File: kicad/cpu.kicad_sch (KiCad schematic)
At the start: 26 parts, among them U1 8288, U2 74LS245, U21 74LS92, U22 74LS245, U23 8087, U24 8088, U28 8237, U29 8255A, U43 74LS74, U45 74LS04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

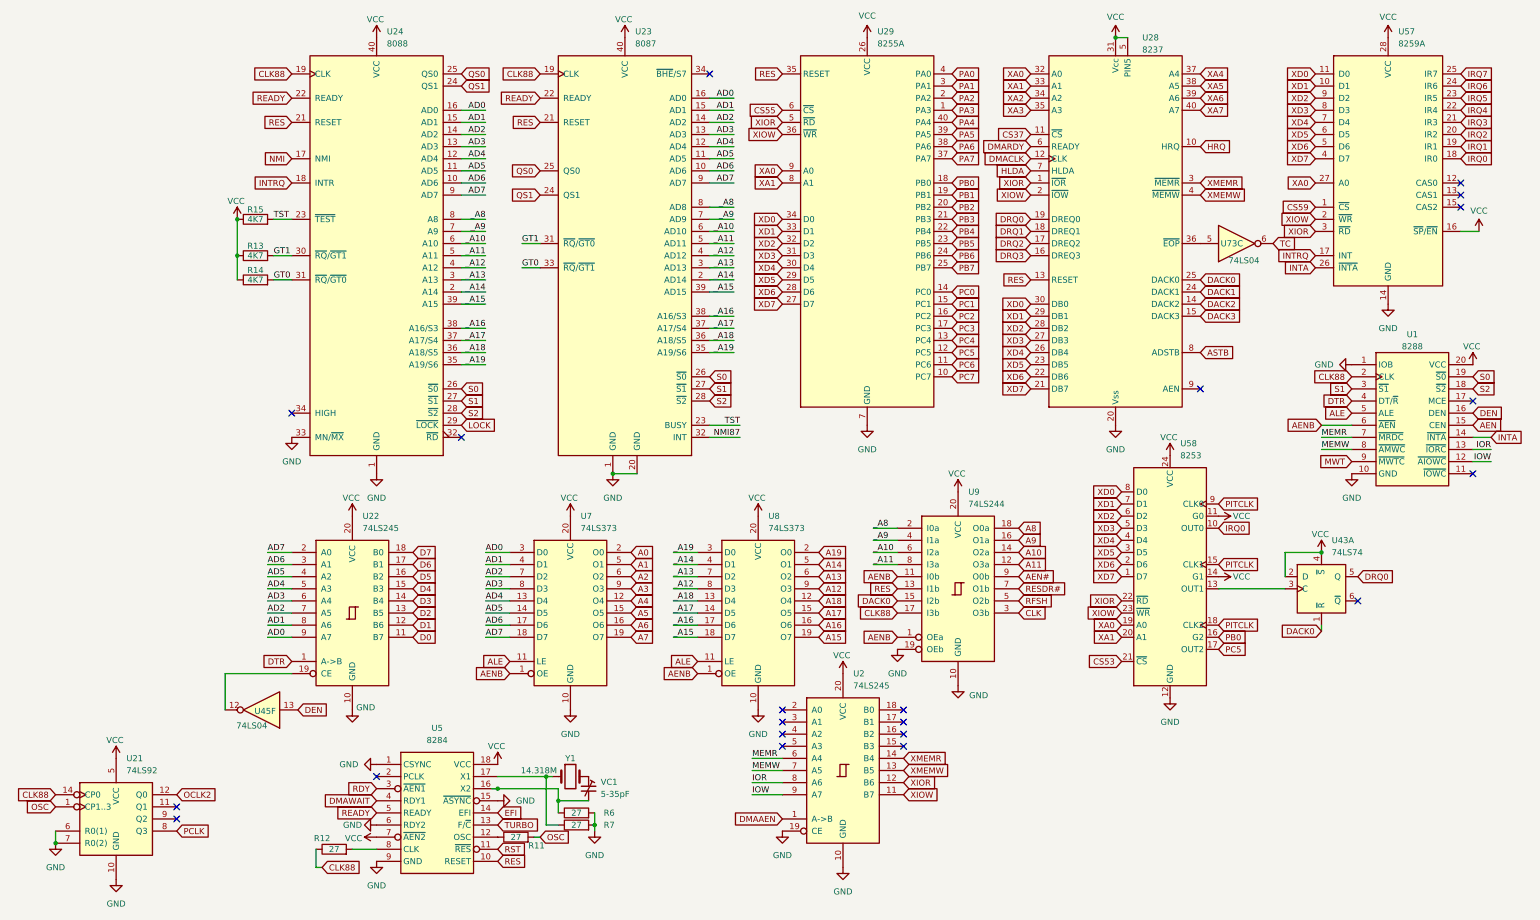
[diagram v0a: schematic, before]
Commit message: finalized schematic
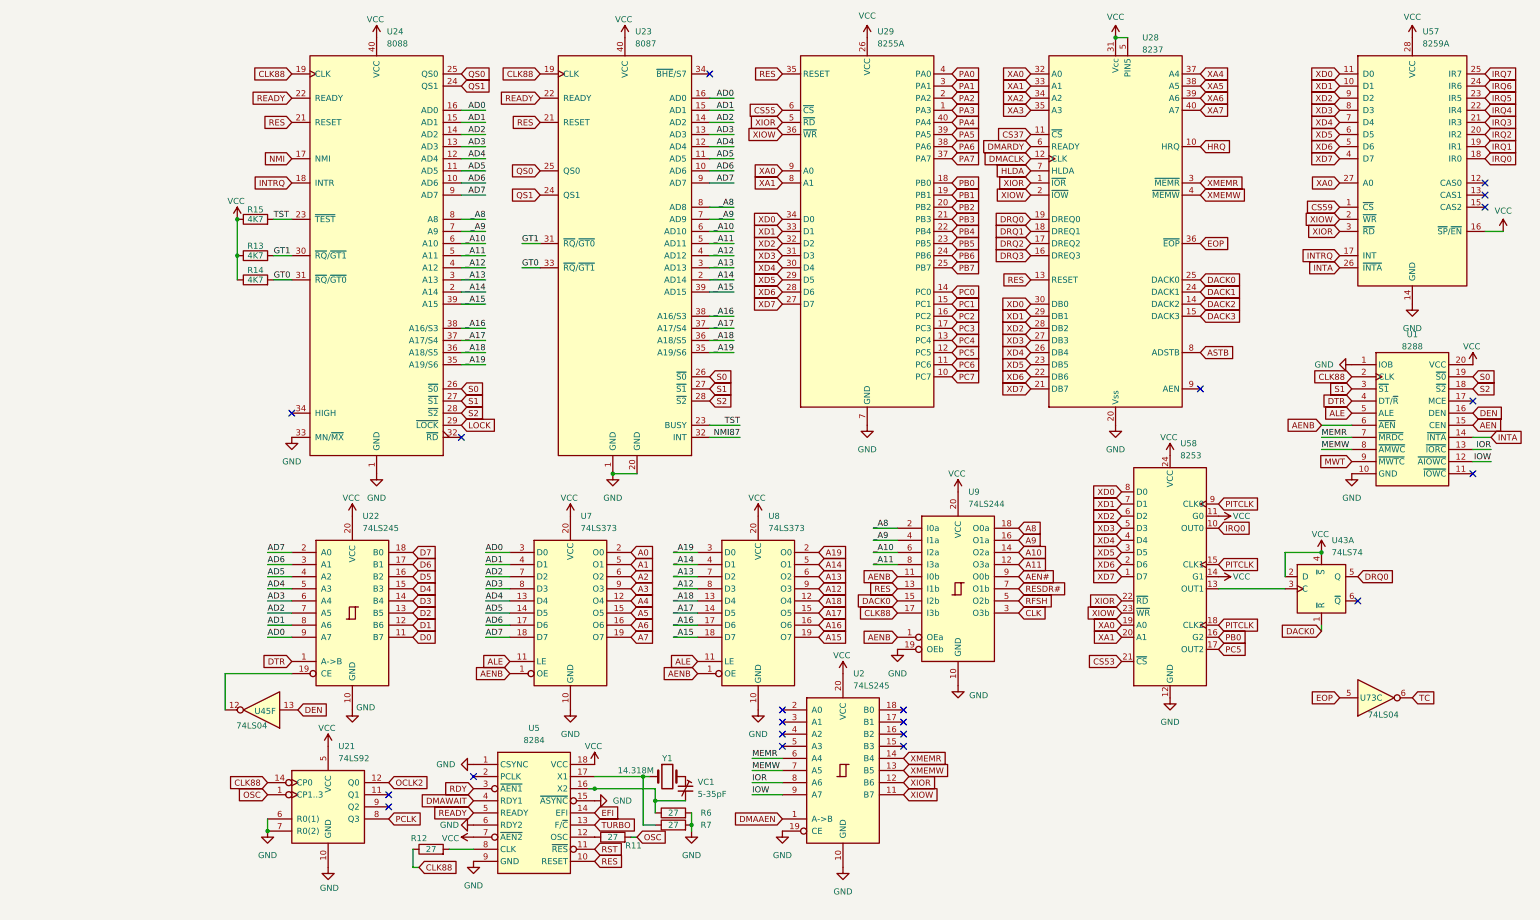
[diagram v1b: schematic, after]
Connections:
- net EOP: now reaches U28.36 (~{EOP}), U73.5
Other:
- moved on the sheet: R11, R12, R6, R7, U21, U5, U57, U73C, VC1, Y1
